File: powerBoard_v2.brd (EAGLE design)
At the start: 23.2 x 34.9 mm, 25 parts, among them U1 TLE2426CD

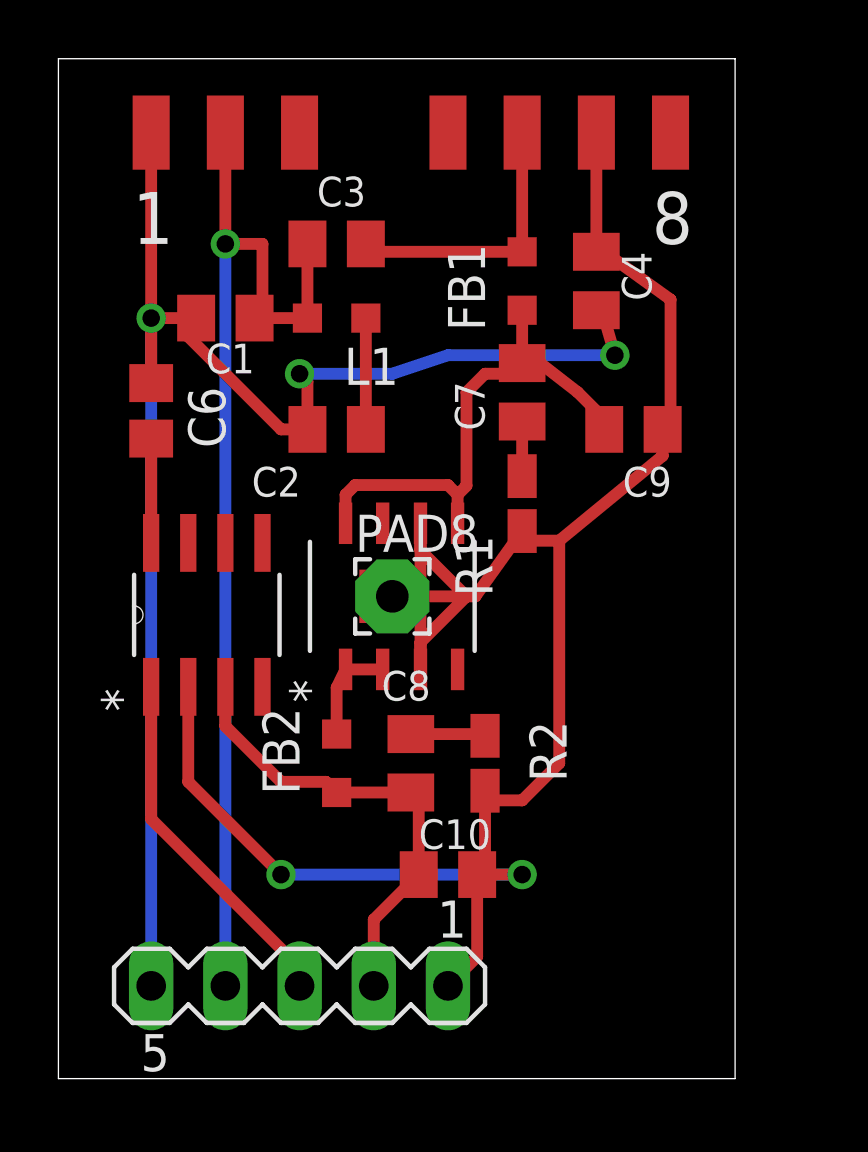
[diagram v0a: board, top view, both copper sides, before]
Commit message: updated power board designs: v2 uses low current 2.5v reference, v3 uses 10v rail and 5v ref both with simple linear regulators. Added breakout board to go from DB37 to BNC
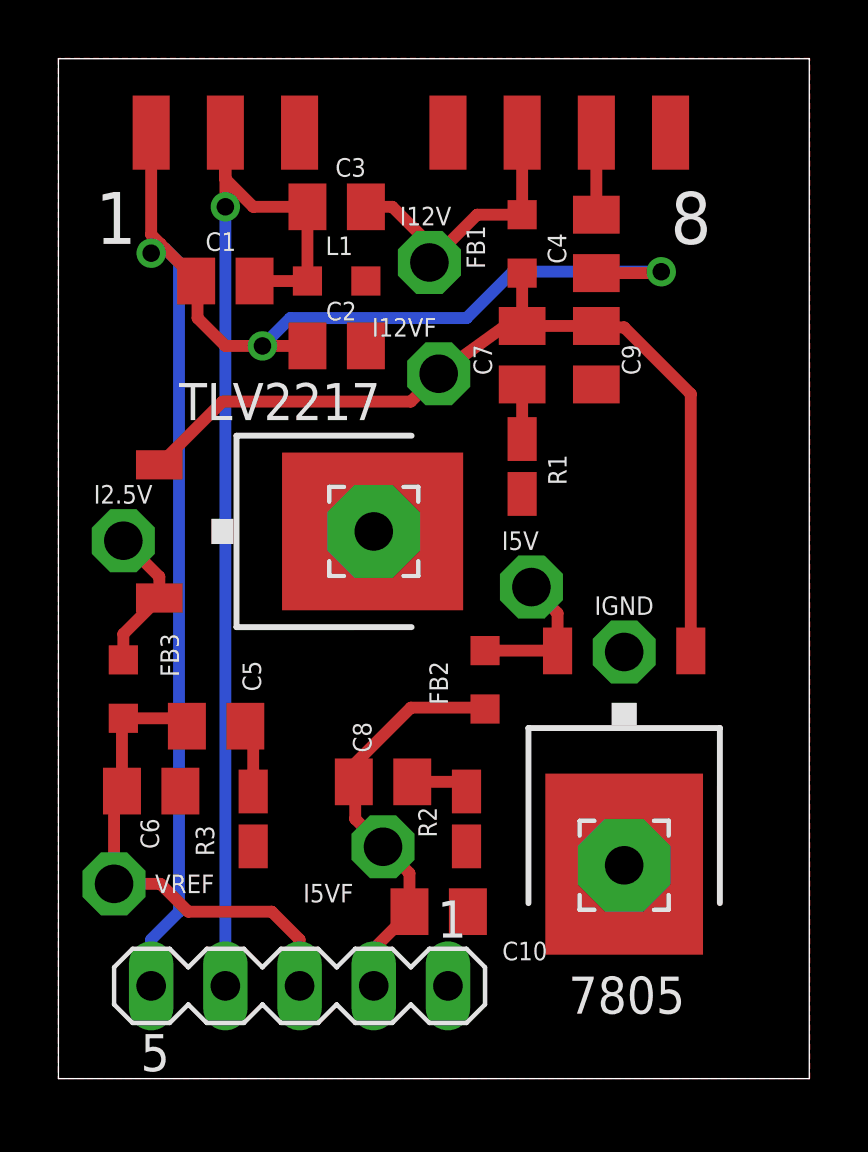
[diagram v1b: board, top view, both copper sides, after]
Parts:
- removed U$1: ADP7105-REGULATOR, tuckerLib:ADP7105-REGULATOR
- removed U1: TLE2426CD, Texas Instruments_By_element14_Batch_1:SOIC127P600X175-8N
- added 7805, TLV2217: 7806DT, linear:TO252
- added C5: 22uf, rcl:C0805K
- added FB3: (no value), rcl:L2012C
- added I12V, I12VF, I2.5V, I5V, I5VF, IGND, VREF: PTR1PAD1-13, testpad:P1-13
- added PAD9: WIREPAD3,17/1,3, wirepad:3,17/1,3
- added R3: 0.33, resistor:R2012W
- C6: value 1uF -> 1uf; device rcl:C0805 -> rcl:C0805K
- PAD8: value (none) -> WIREPAD3,17/1,3; device wirepad:2,54/1,1 -> wirepad:3,17/1,3
- moved C6 13.0 mm to (3.17, 9.84), turned to 0 degrees
- moved PAD8 12.2 mm to (19.4, 7.30)
- moved FB2 5.83 mm to (14.6, 13.7)
- moved C2 2.86 mm to (9.53, 25.1)
- moved C9 2.84 mm to (18.4, 24.8), turned to 270 degrees
- moved R2 2.01 mm to (14.0, 8.89)
- moved C10 1.31 mm to (13.0, 5.71)
- moved C1 1.27 mm to (5.71, 27.3)
- moved C3 1.27 mm to (9.53, 29.8)
- moved C4 1.27 mm to (18.4, 28.6)
- moved C7 1.27 mm to (15.9, 24.8)
- moved FB1 1.27 mm to (15.9, 28.6)
- moved L1 1.27 mm to (9.53, 27.3)
- moved R1 1.27 mm to (15.9, 21.0)
- moved C8 1.14 mm to (11.1, 10.2), turned to 0 degrees
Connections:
- removed net NC3: U$1.4
- removed net PG: U$1.7
- new net VS3+: FB3.1, I2.5V.TP, TLV2217.2
- net GND: no longer C6.2
- net N$2: now also C5.2, R3.2; no longer C6.1, U1.8
- net VREF: now also C5.1, C6.1, FB3.2, VREF.TP; no longer U1.1
- net VS1+: now also I12V.TP
- net VS1-: now also 7805.3, C6.2, IGND.TP, PAD9.1, R3.1, TLV2217.3; no longer U$1.3, U$1.6, U$1.9, U1.2
- net VS1F+: now also 7805.1, I12VF.TP, TLV2217.1; no longer U$1.5, U$1.8
- net VS2+: now also 7805.2, I5V.TP; no longer U$1.1, U$1.2
- net VS2F+: now also I5VF.TP; no longer U1.3
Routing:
- net VS1-: track 72.4 -> 2.81 mm, vias 2 -> 0
- net VS1F+: track 17.9 -> 31.6 mm
- net VS3+: track 0.00 -> 5.10 mm
- net VREF: track 12.3 -> 16.8 mm
- net N$1: track 4.19 -> 0.65 mm
- net VS2F+: track 16.4 -> 14.2 mm
- net VS2+: track 3.55 -> 5.04 mm
- net N$2: track 3.57 -> 2.35 mm
- net GND: track 53.7 -> 54.9 mm
- net VCC: track 37.6 -> 38.4 mm
- net N$3: track 2.56 -> 1.99 mm
- added copper zone on layer 1, net VS1-
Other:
- board size 23.2 x 34.9 mm -> 25.7 x 34.9 mm
